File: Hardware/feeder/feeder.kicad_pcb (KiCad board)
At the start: 2 copper layers, 44.4 x 71.1 mm, 17 parts, among them J1 pump, J2 power, J3 button_set, J4 button_select, J5 button_reset, J6 motor, Q1 BUZ11

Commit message: [WIP] Added some of Benno's improvements
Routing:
- net GND: track 23.0 -> 0.15 mm, vias 1 -> 4
- added copper zone on F.Cu, net GND
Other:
- net class Default: trace_width 0.25 -> 0.5
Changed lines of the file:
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@@
-(kicad_pcb (version 20171130) (host pcbnew 5.1.4)
+(kicad_pcb (version 20171130) (host pcbnew 5.0.2+dfsg1-1)
   (general
     (thickness 1.6)
     (drawings 57)
-    (tracks 72)
+    (tracks 64)
     (zones 0)
     (modules 17)
@@
   )
   (setup
-    (last_trace_width 0.25)
+    (last_trace_width 0.5)
     (trace_clearance 0.2)
     (zone_clearance 0.508)
     (zone_45_only no)
     (trace_min 0.2)
+    (segment_width 0.2)
+    (edge_width 0.05)
     (via_size 0.8)
     (via_drill 0.4)
@@
     (uvia_min_size 0.2)
     (uvia_min_drill 0.1)
-    (edge_width 0.05)
-    (segment_width 0.2)
     (pcb_text_width 0.3)
     (pcb_text_size 1.5 1.5)
@@
   (net_class Default "This is the default net class."
     (clearance 0.2)
-    (trace_width 0.25)
+    (trace_width 0.5)
     (via_dia 0.8)
     (via_drill 0.4)
@@
   (segment (start 139.7 123.19) (end 132.08 130.81) (width 0.25) (layer F.Cu) (net 9))
   (segment (start 134.62 123.19) (end 139.7 123.19) (width 0.25) (layer F.Cu) (net 9))
-  (via (at 127 140.97) (size 0.8) (drill 0.4) (layers F.Cu B.Cu) (net 22))
-  (segment (start 128.6 139.37) (end 128.6 138.27) (width 0.25) (layer F.Cu) (net 22))
-  (segment (start 127 140.97) (end 128.6 139.37) (width 0.25) (layer F.Cu) (net 22))
   (segment (start 122.7 138.37) (end 122.55 138.37) (width 0.25) (layer F.Cu) (net 22))
-  (segment (start 124.474999 140.144999) (end 122.7 138.37) (width 0.25) (layer F.Cu) (net 22))
-  (segment (start 126.174999 140.144999) (end 124.474999 140.144999) (width 0.25) (layer F.Cu) (net 22))
-  (segment (start 127 140.97) (end 126.174999 140.144999) (width 0.25) (layer F.Cu) (net 22))
-  (segment (start 124.15 143.82) (end 122.55 143.82) (width 0.25) (layer F.Cu) (net 22))
-  (segment (start 127 140.97) (end 124.15 143.82) (width 0.25) (layer F.Cu) (net 22))
-  (segment (start 129.85 143.82) (end 127 140.97) (width 0.25) (layer F.Cu) (net 22))
-  (segment (start 131.45 143.82) (end 129.85 143.82) (width 0.25) (layer F.Cu) (net 22))
-  (segment (start 131.35 138.27) (end 131.45 138.37) (width 0.25) (layer F.Cu) (net 22))
-  (segment (start 128.6 138.27) (end 131.35 138.27) (width 0.25) (layer F.Cu) (net 22))
+  (via (at 119.38 138.43) (size 0.8) (drill 0.4) (layers F.Cu B.Cu) (net 22))
+  (via (at 134.62 138.43) (size 0.8) (drill 0.4) (layers F.Cu B.Cu) (net 22))
+  (via (at 134.62 143.51) (size 0.8) (drill 0.4) (layers F.Cu B.Cu) (net 22))
+  (via (at 119.38 143.51) (size 0.8) (drill 0.4) (layers F.Cu B.Cu) (net 22))
   (segment (start 140.97 98.94) (end 140.97 97.79) (width 0.25) (layer B.Cu) (net 24))
   (segment (start 147.44 105.41) (end 140.97 98.94) (width 0.25) (layer B.Cu) (net 24))
@@
   (segment (start 133.820001 118.580001) (end 134.62 119.38) (width 0.25) (layer F.Cu) (net 33))
   (segment (start 124.46 105.41) (end 125.635001 106.585001) (width 0.25) (layer F.Cu) (net 33))
-  (segment (start 146.05 119.38) (end 154.94 110.49) (width 0.25) (layer F.Cu) (net 33))
-  (segment (start 134.62 119.38) (end 146.05 119.38) (width 0.25) (layer F.Cu) (net 33))
+  (segment (start 146.05 119.38) (end 154.94 110.49) (width 0.25) (layer F.Cu) (net 33) (status 1000000))
+  (segment (start 134.62 119.38) (end 146.05 119.38) (width 0.25) (layer F.Cu) (net 33) (status 1000000))
   (zone (net 22) (net_name GND) (layer B.Cu) (hatch edge 0.508)
     (connect_pads (clearance 0.508))
@@
     (polygon
       (pts
-        (xy 114.3 77.47) (xy 114.3 146.05) (xy 156.21 146.05) (xy 156.21 77.47)
+        (xy 113.03 76.2) (xy 113.03 147.32) (xy 157.48 147.32) (xy 157.48 76.2)
       )
     )
+  )
+  (zone (net 22) (net_name GND) (layer F.Cu) (hatch edge 0.508)
+    (connect_pads (clearance 0.508))
+    (min_thickness 0.254)
+    (fill yes (arc_segments 16) (thermal_gap 0.508) (thermal_bridge_width 0.508))
+    (polygon
+      (pts
+        (xy 113.03 76.2) (xy 157.48 76.2) (xy 157.48 147.32) (xy 113.03 147.32)
+      )
+    )

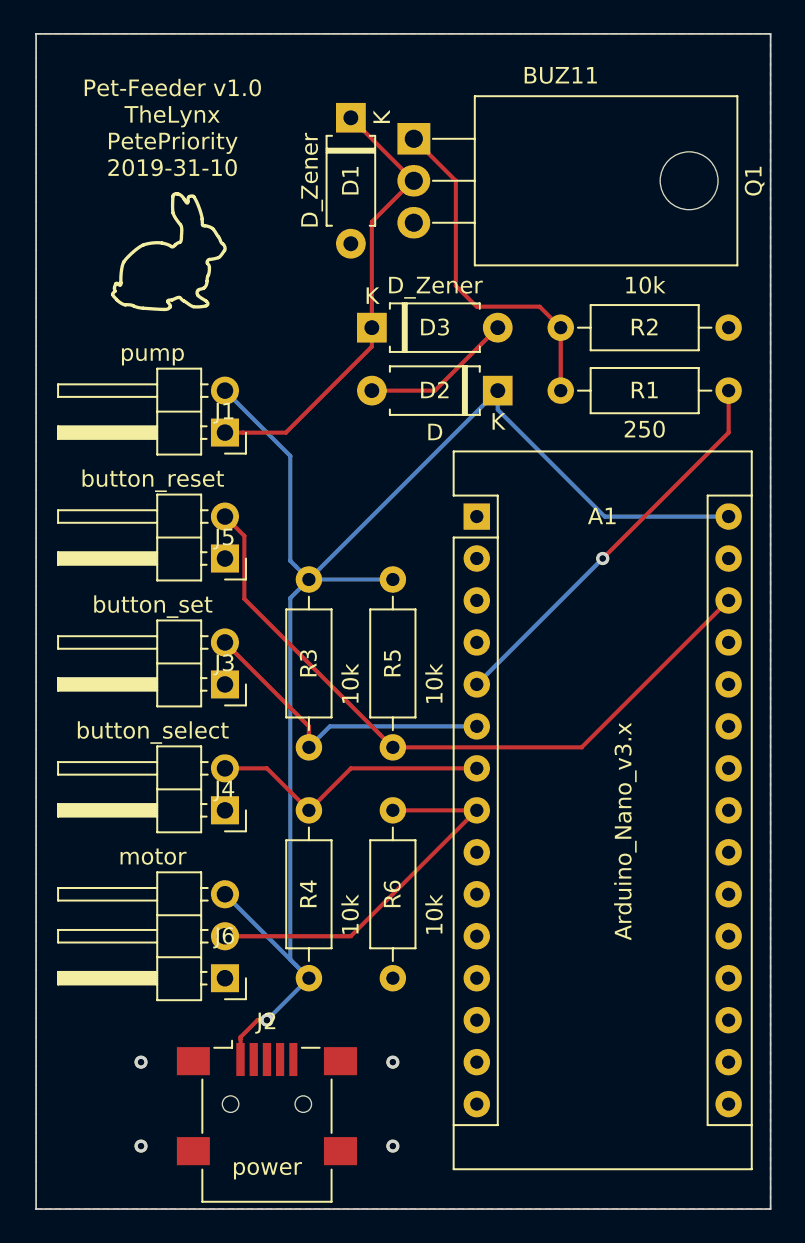
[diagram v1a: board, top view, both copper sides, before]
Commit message: More of Benno's improvements
* Increased track width to .5mm
* Added ground plane on front
* Placed multiple vias connecting both ground planes across board
* Minor schematic clean up
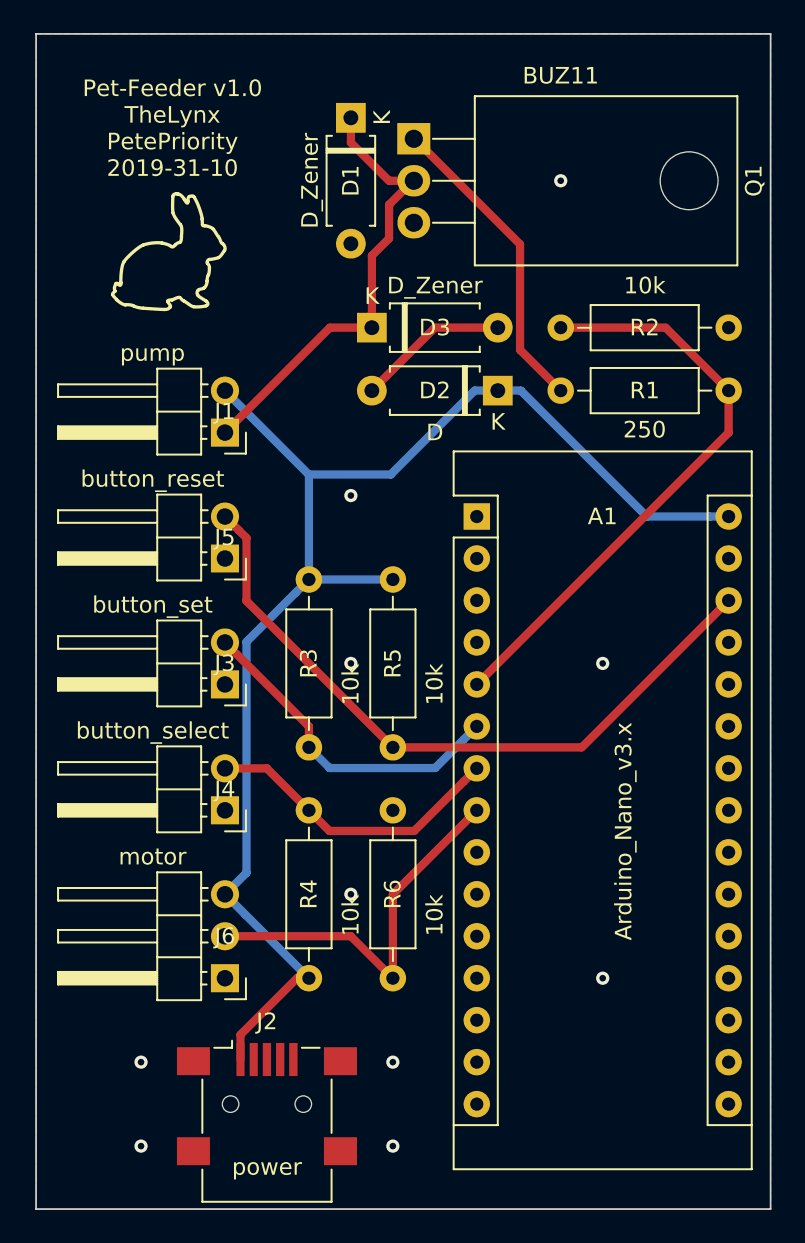
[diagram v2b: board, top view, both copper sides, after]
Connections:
- R2 pad 1: Net-(Q1-Pad1) -> /signal_pump
- R6 pad 1: /signal_motor -> GND
- R6 pad 2: GND -> /signal_motor
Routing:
- net /signal_pump: track 24.1 -> 35.8 mm, vias 1 -> 0
- net +5V: track 91.8 -> 84.7 mm, vias 1 -> 0
- net Net-(Q1-Pad1): track 21.2 -> 19.0 mm
- net /signal_button_set: track 19.1 -> 20.2 mm
- net /signal_button_select: track 17.3 -> 18.4 mm
- net GND: vias 4 -> 10

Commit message: Added capacitors to power supply
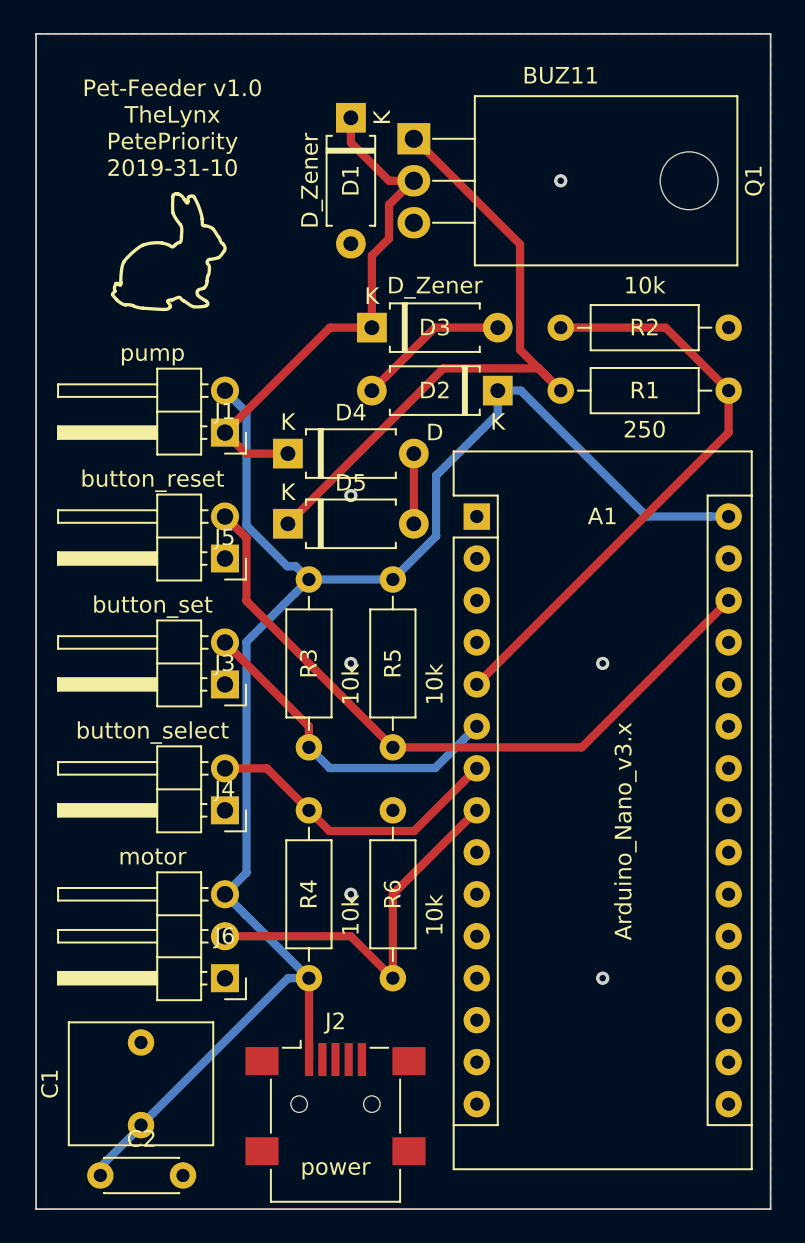
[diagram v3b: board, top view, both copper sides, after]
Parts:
- added C1: 4.7uF, Capacitor_THT:C_Rect_L7.2mm_W8.5mm_P5.00mm_FKP2_FKP2_MKS2_MKP2, F.Cu at (119.4, 142.2)
- added C2: 100nF, Capacitor_THT:C_Disc_D4.3mm_W1.9mm_P5.00mm, F.Cu at (116.9, 145.3)
- added D4: D_Zener, Diode_THT:D_A-405_P7.62mm_Horizontal, F.Cu at (128.3, 101.6)
- added D5: D_Zener, Diode_THT:D_A-405_P7.62mm_Horizontal, F.Cu at (128.3, 105.8)
- moved J2 4.15 mm to (131.2, 141.0)
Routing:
- net Net-(D5-Pad1): track 19.0 -> 39.9 mm
- net +5V: track 84.7 -> 100.8 mm
- net Net-(D1-Pad1): track 27.8 -> 32.1 mm
- net Net-(D4-Pad2): track 0.00 -> 4.25 mm
- net GND: track 0.15 -> 0.00 mm, vias 10 -> 6
